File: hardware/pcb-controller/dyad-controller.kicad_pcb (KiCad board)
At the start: 2 copper layers, 35 x 57 mm, 44 parts, among them J1 USB_C_Receptacle_USB2.0, J10 USB-C split link, J6 HC-FPC-0.5-20P-FH20, J7 HC-FPC-0.5-20P-FH20, J8 HC-FPC-0.5-14P-FH20, J9 USB-C split link, SW1 BOOTSEL, SW2 RESET, U1 W25Q128JVS, U2 USBLC6-2SC6, U3 RP2040, U4 XC6206PxxxMR-Regulator_Linear, Y1 12MHz

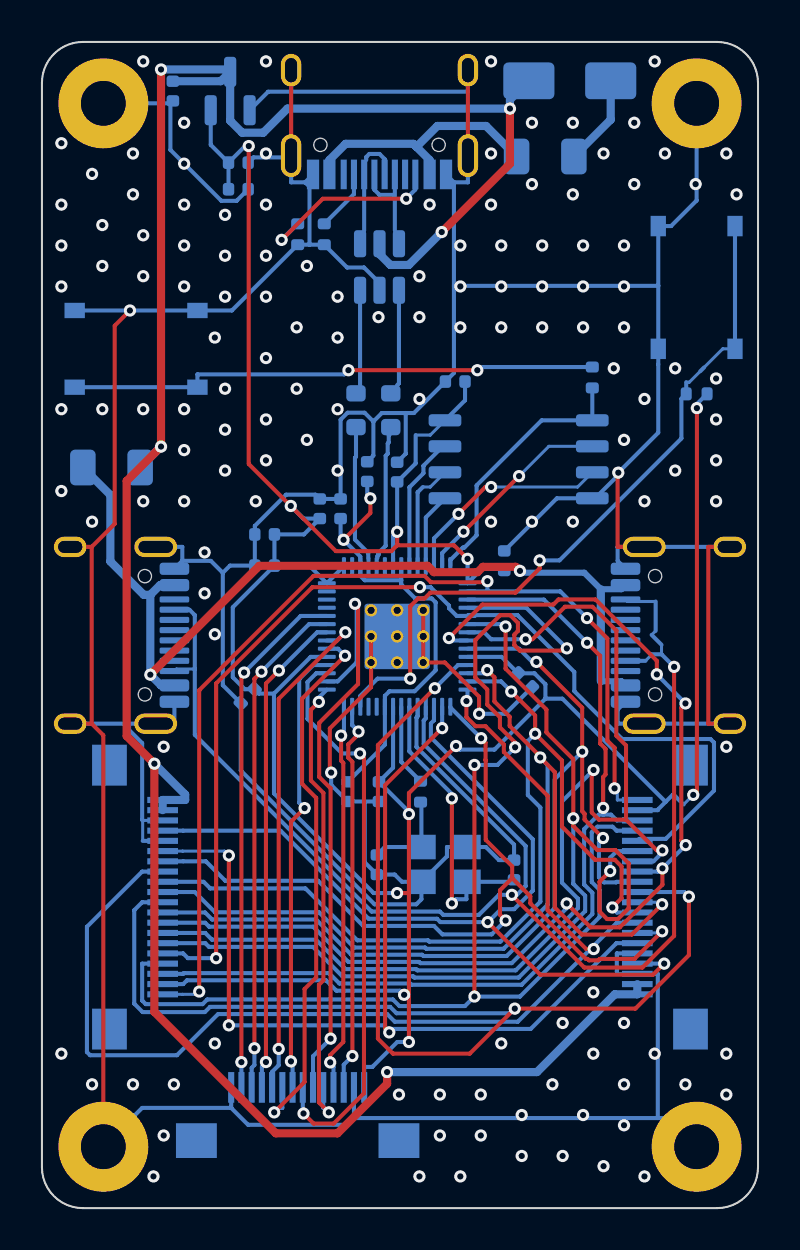
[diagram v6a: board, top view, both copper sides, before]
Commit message: Hand-reroute around the crystal to improve its ground and the B.Cu fill
Rerouted by hand in KiCad: GPIO2, GPIO4, GPIO5, GPIO7, GPIO9, GPIO12,
GPIO15, +3V3 and XTAL_IN. No parts moved; USB untouched (D+ 15.9 / D- 16.1
mm, B.Cu, no vias).

Against fce0c60: ground under the crystal (GND fill on the opposite layer
along its tracks) 46% -> 54%; B.Cu fill 52% -> 54% in 6 pieces instead of
7, main piece 994 -> 1,018 mm^2. USB 82% and QSPI 65% unchanged; F.Cu fill
65%, main piece 1,149 -> 1,146 mm^2. CONTROLLER.md §6 figures updated.

DRC: 0 errors, 0 unconnected, nothing dangling (unchanged by a refill).
Parity: 14.

Co-Authored-By: Claude Opus 5.5 <noreply@anthropic.com>
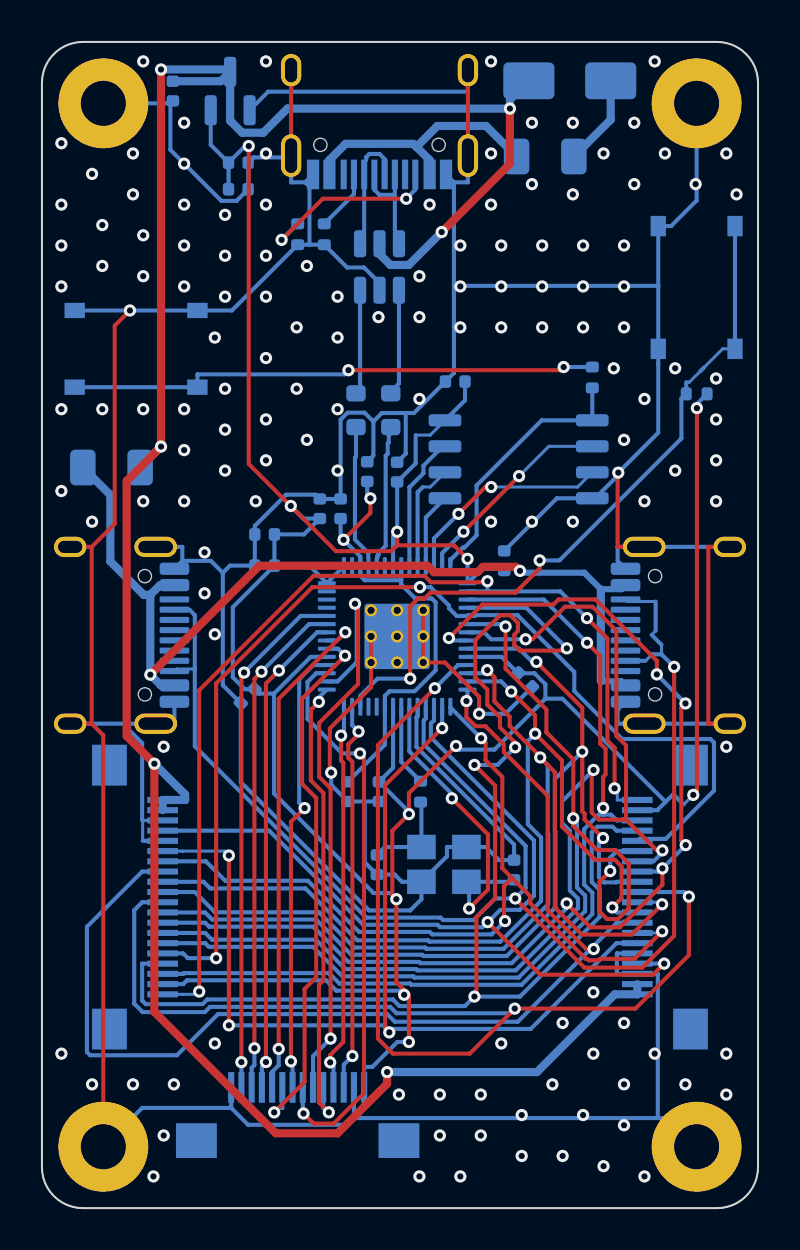
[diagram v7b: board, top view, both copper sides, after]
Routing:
- net XTAL_IN: track 14.5 -> 15.6 mm
- net /GPIO2: track 66.0 -> 66.8 mm
- net GND: track 339.2 -> 339.8 mm

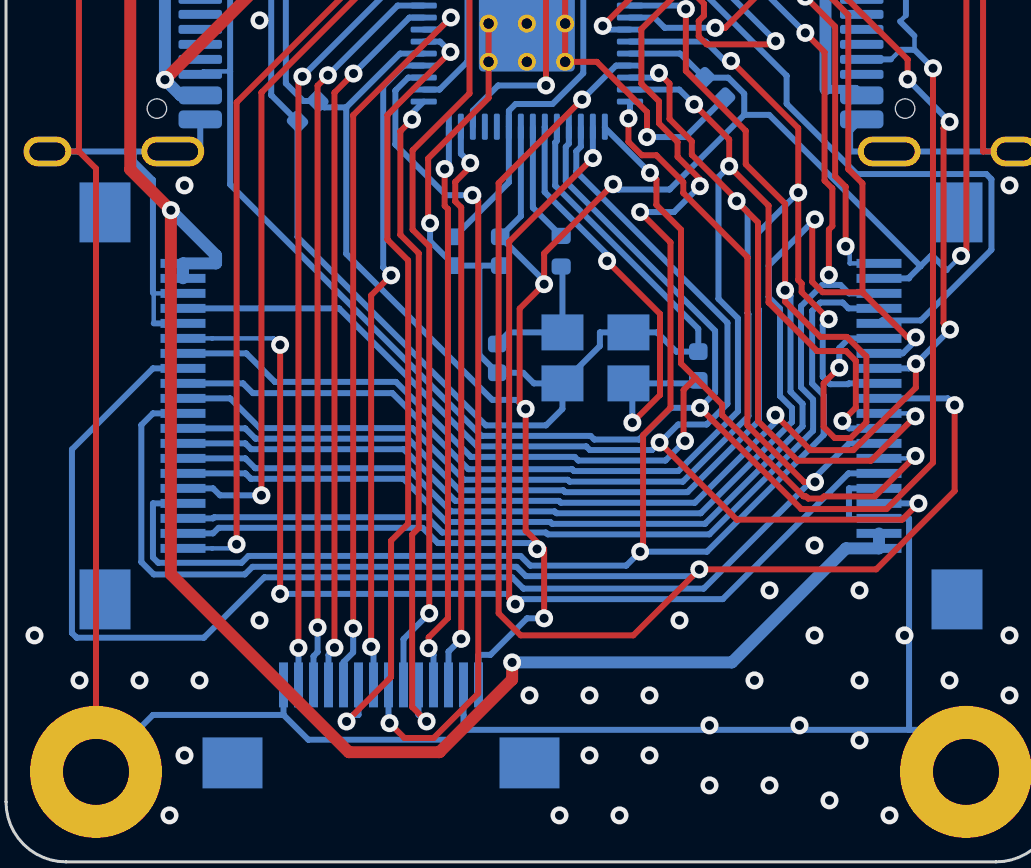
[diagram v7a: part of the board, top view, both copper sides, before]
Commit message: Hand-reroute +3V3, GPIO2, GPIO8 and GPIO13 to join the F.Cu fill
Rerouted by hand in KiCad. No parts moved; USB untouched.

Against 5744557: F.Cu GND fill 65% -> 66% of the board in 3 pieces instead
of 4, main piece 1,146 -> 1,242 mm^2. B.Cu 54% -> 53%, main piece 1,018 ->
1,014 mm^2. Ground under USB / QSPI / crystal unchanged at 82% / 65% / 54%.

DRC: 0 errors, 0 unconnected, nothing dangling. Parity: 14.

Co-Authored-By: Claude Opus 5.5 <noreply@anthropic.com>
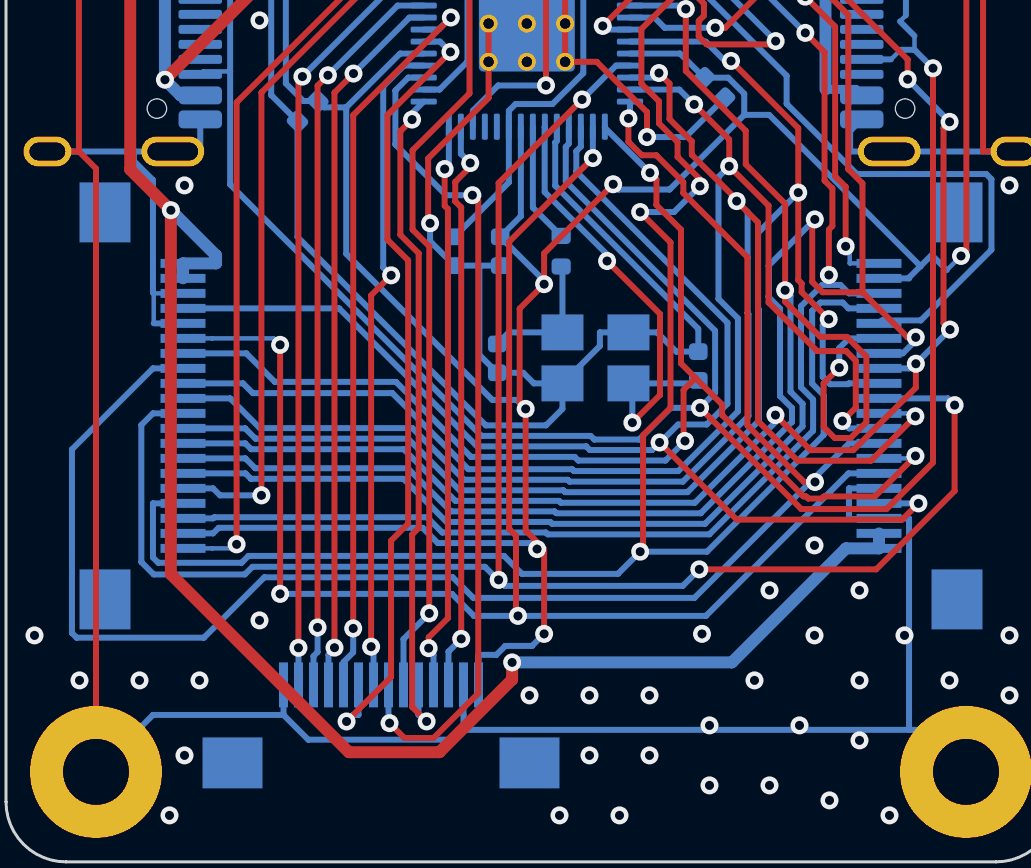
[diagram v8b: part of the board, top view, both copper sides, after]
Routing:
- net /GPIO8: track 68.5 -> 60.0 mm, vias 3 -> 4
- net /GPIO13: track 50.7 -> 51.6 mm
